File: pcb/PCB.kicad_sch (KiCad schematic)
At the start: 23 parts, among them J1 TE 770966-2, J2 TE 770966-2, J3 JST B04B-XASK, K1 AZDC6, K2 dbt71205u21, Q1 IRLZ44N, U1 LM339, U2 LTV-817S, U3 VRB1205YMD-15WR3

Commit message: Added mounting holes and fixed drc violations
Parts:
- added H1, H2, H3: MountingHole, MountingHole:MountingHole_3.2mm_M3, symbol Mechanical:MountingHole
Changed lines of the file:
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@@
     (pin "1")
+  )
+  (symbol (lib_id "Mechanical:MountingHole") (at 209.55 119.38 0) (unit 1)
+    (in_bom yes) (on_board yes)
+    (property "Reference" "H2" (id 0) (at 209.55 114.3 0))
+    (property "Value" "MountingHole" (id 1) (at 209.55 116.205 0))
+    (property "Footprint" "MountingHole:MountingHole_3.2mm_M3" (id 2) (at 209.55 119.38 0)
+      (effects (font (size 1.27 1.27)) hide)
+    )
+    (property "Datasheet" "~" (id 3) (at 209.55 119.38 0)
+      (effects (font (size 1.27 1.27)) hide)
+    )
   )
   (symbol (lib_id "VRB1205YMD-6WR3:VRB1205YMD-15WR3") (at 156.21 82.55 0) (mirror y) (unit 1)
@@
     )
     (pin "1")
+  )
+  (symbol (lib_id "Mechanical:MountingHole") (at 209.55 110.49 0) (unit 1)
+    (in_bom yes) (on_board yes) (fields_autoplaced)
+    (property "Reference" "H1" (id 0) (at 212.09 109.2199 0)
+      (effects (font (size 1.27 1.27)) (justify left))
+    )
+    (property "Value" "MountingHole" (id 1) (at 212.09 111.7599 0)
+      (effects (font (size 1.27 1.27)) (justify left))
+    )
+    (property "Footprint" "MountingHole:MountingHole_3.2mm_M3" (id 2) (at 209.55 110.49 0)
+      (effects (font (size 1.27 1.27)) hide)
+    )
+    (property "Datasheet" "~" (id 3) (at 209.55 110.49 0)
+      (effects (font (size 1.27 1.27)) hide)
+    )
   )
   (symbol (lib_id "power:+5V") (at 132.08 29.21 0) (unit 1)
@@
     (pin "3")
   )
+  (symbol (lib_id "Mechanical:MountingHole") (at 209.55 128.27 0) (unit 1)
+    (in_bom yes) (on_board yes)
+    (property "Reference" "H3" (id 0) (at 209.55 123.19 0))
+    (property "Value" "MountingHole" (id 1) (at 209.55 125.095 0))
+    (property "Footprint" "MountingHole:MountingHole_3.2mm_M3" (id 2) (at 209.55 128.27 0)
+      (effects (font (size 1.27 1.27)) hide)
+    )
+    (property "Datasheet" "~" (id 3) (at 209.55 128.27 0)
+      (effects (font (size 1.27 1.27)) hide)
+    )
+  )
   (sheet_instances
     (path "/" (page "1"))
@@
       (reference "D2") (unit 1) (value "SMAJ15CA") (footprint "Diode_SMD:D_SMA")
     )
+    (path "/cf50b2c5-84f5-4b3c-a991-b977840bebe8"
+      (reference "H1") (unit 1) (value "MountingHole") (footprint "MountingHole:MountingHole_3.2mm_M3")
+    )
+    (path "/77378485-b21c-47c0-8422-4507bb2f71fe"
+      (reference "H2") (unit 1) (value "MountingHole") (footprint "MountingHole:MountingHole_3.2mm_M3")
+    )
+    (path "/fbc4413b-7039-4267-b22c-9a7b4c3f37be"
+      (reference "H3") (unit 1) (value "MountingHole") (footprint "MountingHole:MountingHole_3.2mm_M3")
+    )
     (path "/37ff6ad9-a0e8-44b4-a71c-e54f0b1e1063"

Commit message: Final? Pre/Dis
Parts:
- added C2, C3: 100u, Capacitor_SMD:CP_Elec_6.3x7.7, symbol Device:C_Polarized_Small
- added D3: SMAJ15CA, Diode_SMD:D_SMA, symbol Device:D_TVS
- added D4: ssb43L, Diode_SMD:D_SMB, symbol Device:D_Schottky
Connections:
- net +12V: now also C3.1, D3.2 (A2), D4.1 (K)
- net +5V: now also C2.1
- net AIR: now also D4.2 (A)
- net GND: now also C3.2, D3.1 (A1)
- net TS-: now also C2.2

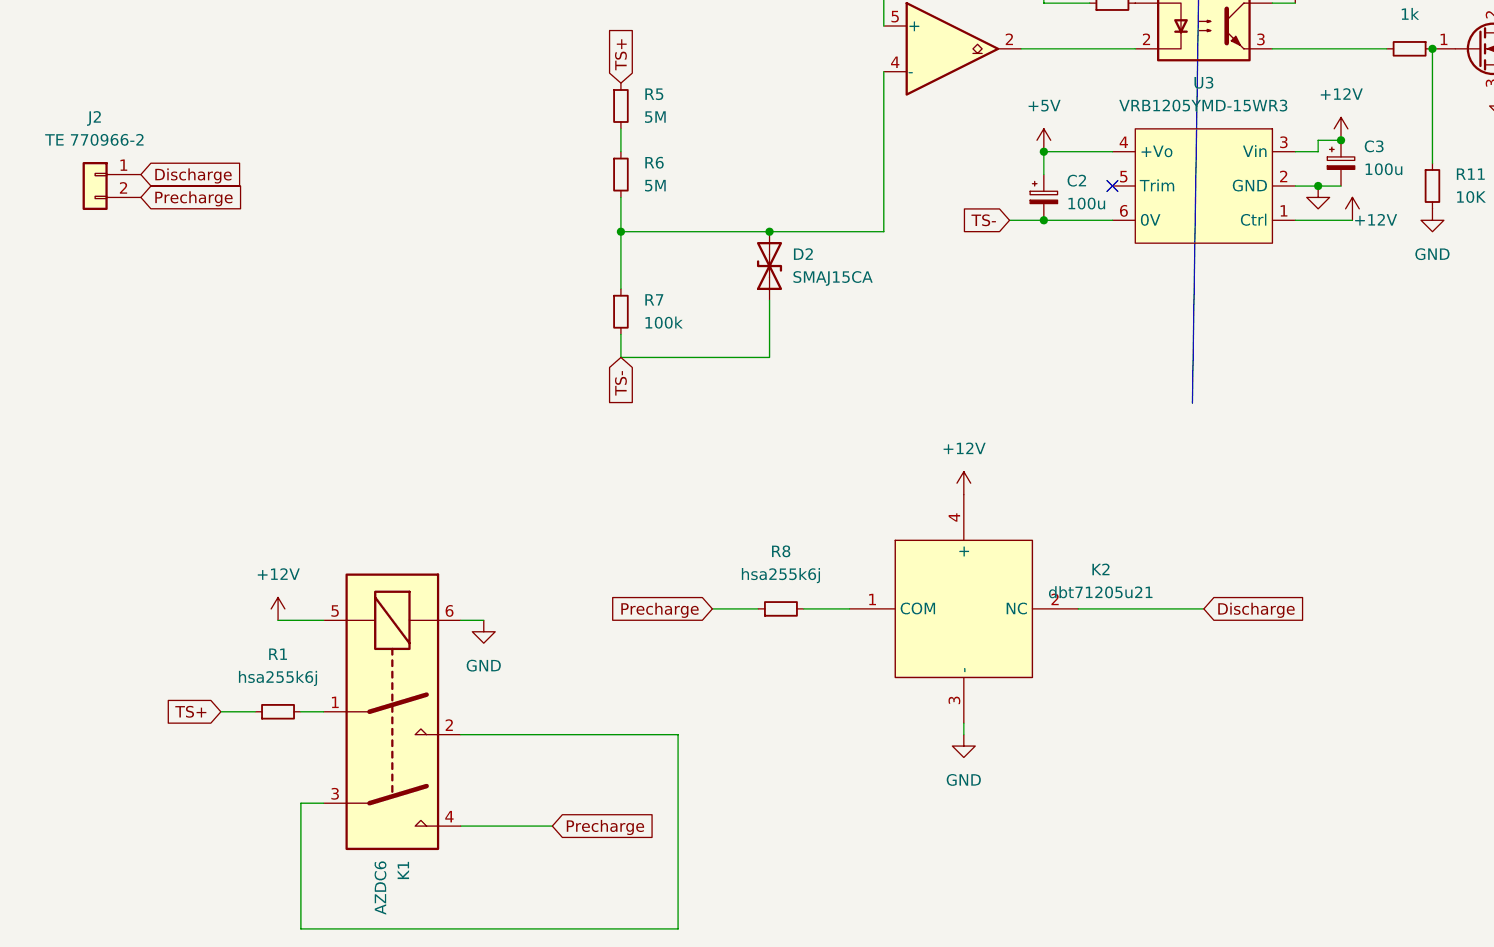
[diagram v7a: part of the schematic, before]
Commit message: Precharge W/o Discharge
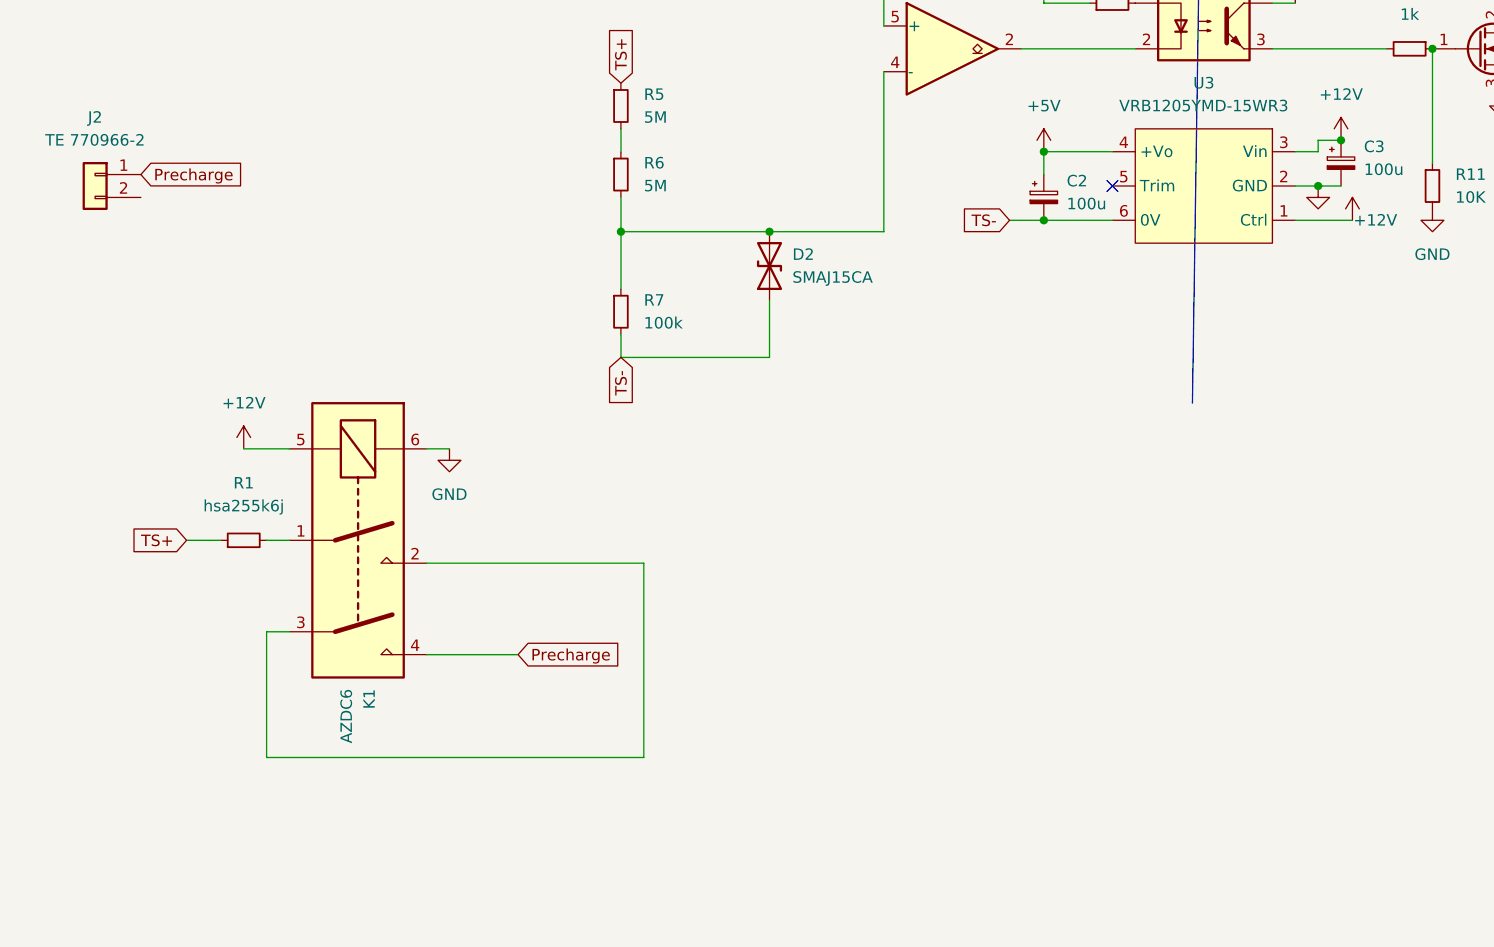
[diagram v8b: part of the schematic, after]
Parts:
- removed K2: dbt71205u21, dbt71205u:DBT71205U, symbol dbt71205u2:dbt71205u21
- removed R8: hsa255k6j, hsa255k6j:hsa255k6j, symbol Device:R_Small
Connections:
- net Discharge is gone; now on net Precharge: J2.1 (Pin_1)
- net Precharge: no longer J2.2 (Pin_2)
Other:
- moved on the sheet: K1, R1
